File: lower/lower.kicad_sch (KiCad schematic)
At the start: 4 parts

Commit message: Lower v0.1.0. Pre-routing
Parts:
- added B1: board-outline, lower-all:board-outline-test, symbol lower-all:board-outline
- added D1: 2.7V, Diode_THT:D_T-1_P5.08mm_Horizontal, symbol Device:D_Zener
- added D2: 1N4007, Diode_THT:D_DO-41_SOD81_P10.16mm_Horizontal, symbol Diode:1N4007
- added ESCWires1, ESCWires2, ESCWires3, ESCWires4: ~, lower-all:WireESC, symbol lower-all:WireESC
- added M1, M2, M3, M4: MotorCutout, lower-all:MotorEdges, symbol lower-all:Motor
- added MotorWires1, MotorWires2, MotorWires3, MotorWires4: ~, lower-all:WireMotor, symbol lower-all:WireMotor
- added R1: 510, Resistor_SMD:R_0201_0603Metric_Pad0.64x0.40mm_HandSolder, symbol Device:R
- added R2: 33, Resistor_THT:R_Axial_DIN0207_L6.3mm_D2.5mm_P7.62mm_Horizontal, symbol Device:R
- added R3: 470, Resistor_THT:R_Axial_DIN0207_L6.3mm_D2.5mm_P7.62mm_Horizontal, symbol Device:R
- added SW1: SW_SPDT, Button_Switch_THT:SW_Slide_SPDT_Angled_CK_OS102011MA1Q, symbol Switch:SW_SPDT
- added TP1: Psense, TestPoint:TestPoint_2Pads_Pitch2.54mm_Drill0.8mm, symbol Connector:TestPoint_2Pole
- added U1: BTS50080-1TMA, Package_TO_SOT_SMD:TO-263-7_TabPin4, symbol Power_Management:BTS50080-1TMA
- added WireBatt1: ~, lower-all:WireBatt, symbol lower-all:WireBatt
- added WireESCPwr1, WireESCPwr2, WireESCPwr3, WireESCPwr4: ~, lower-all:WireESCPwr, symbol lower-all:WireESCPwr
- H1, H2, H3, H4: value MountingHole_Pad -> MountingHole; symbol Mechanical:MountingHole_Pad -> Mechanical:MountingHole
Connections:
- new net: SW1.2 (B), U1.3 (IN)
- new net: D2.2 (A), U1.5 (IS)
- new net: R2.2, R3.1
- new net A1: ESCWires1.1 (Red), MotorWires1.1 (Upper)
- new net A2: ESCWires2.1 (Red), MotorWires2.3 (Lower)
- new net A3: ESCWires3.1 (Red), MotorWires3.3 (Lower)
- new net A4: ESCWires4.1 (Red), MotorWires4.1 (Upper)
- new net B1: ESCWires1.2 (Blue), MotorWires1.2 (Middle)
- new net B2: ESCWires2.2 (Blue), MotorWires2.2 (Middle)
- new net B3: ESCWires3.2 (Blue), MotorWires3.2 (Middle)
- new net B4: ESCWires4.2 (Blue), MotorWires4.2 (Middle)
- new net C1: ESCWires1.3 (Black), MotorWires1.3 (Lower)
- new net C2: ESCWires2.3 (Black), MotorWires2.1 (Upper)
- new net C3: ESCWires3.3 (Black), MotorWires3.1 (Upper)
- new net C4: ESCWires4.3 (Black), MotorWires4.3 (Lower)
- new net GND: D1.2 (A), R1.2, R3.2, SW1.1 (A), TP1.2, WireBatt1.2 (Black), WireESCPwr1.2 (Black), WireESCPwr2.2 (Black), WireESCPwr3.2 (Black), WireESCPwr4.2 (Black)
- new net Psense: D1.1 (K), D2.1 (K), R1.1, R2.1, TP1.1
- new net Vbb: U1.4 (Vbb), WireBatt1.1 (Red)
- new net Vcc: U1.1 (OUT), U1.2 (OUT), U1.6 (OUT), U1.7 (OUT), WireESCPwr1.1 (Red), WireESCPwr2.1 (Red), WireESCPwr3.1 (Red), WireESCPwr4.1 (Red)
- no-connect marks 0 -> 1
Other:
- note added: "TODO: * Route * Redo frame shape"

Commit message: Lower v0.1.1. Pre-routing
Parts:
- added JP1: Jumper_2_Bridged, lower-all:SolderJumperLarge, symbol Jumper:Jumper_2_Bridged
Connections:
- net GND: now also JP1.2 (B); no longer WireBatt1.2 (Black), WireESCPwr1.2 (Black), WireESCPwr2.2 (Black), WireESCPwr3.2 (Black), WireESCPwr4.2 (Black)
- new net GNDPWR: JP1.1 (A), WireBatt1.2 (Black), WireESCPwr1.2 (Black), WireESCPwr2.2 (Black), WireESCPwr3.2 (Black), WireESCPwr4.2 (Black)
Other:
- note added: "TODO: * Fix rotor placement * Route * Redo frame shape"
- note removed: "TODO: * Route * Redo frame shape"
- moved on the sheet: B1, D1, D2, ESCWires1, ESCWires2, ESCWires3, ESCWires4, M1, M2, M3, M4, MotorWires1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

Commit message: Lower v0.1.2. Pre-routing
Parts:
- renumbered WireBatt1 to Batt1
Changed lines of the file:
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@@
 		(dnp no)
 		(fields_autoplaced yes)
-		(property "Reference" "WireBatt1"
+		(property "Reference" "Batt1"
 			(at 245.11 24.13 0)
 			(do_not_autoplace yes)
@@
 			(project ""
 				(path "/38495dd5-5138-4faa-88d9-26986d1150e3"
-					(reference "WireBatt1")
+					(reference "Batt1")
 					(unit 1)
 				)

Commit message: Upper/Lower: v0.2.0. Pre-routed
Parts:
- added R4, R5: 0, Resistor_SMD:R_1206_3216Metric_Pad1.30x1.75mm_HandSolder, symbol Device:R
- added R6, R7: 0, Resistor_THT:R_Axial_DIN0207_L6.3mm_D2.5mm_P7.62mm_Horizontal, symbol Device:R
- added TP2: Vsense, TestPoint:TestPoint_2Pads_Pitch2.54mm_Drill0.8mm, symbol Connector:TestPoint_2Pole
- TP1: value Psense -> Isense
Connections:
- net GND: now also R5.1, R7.2, TP2.2
- net Vcc: now also R4.1, R6.1
- net Psense renamed Isense
- new net _Vsense: R4.2, R5.2, R6.2, R7.1, TP2.1

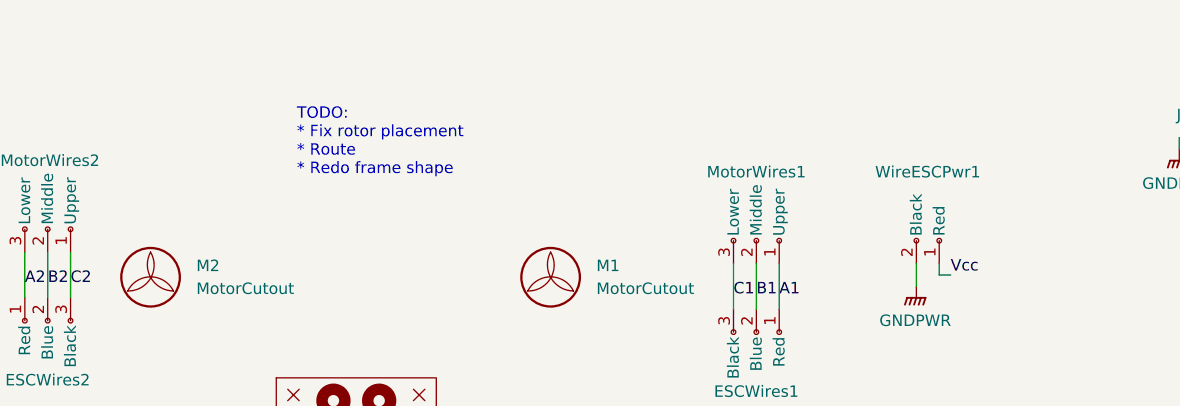
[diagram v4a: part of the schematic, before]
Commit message: Upper/Lower: Add post-assembly fixup comments
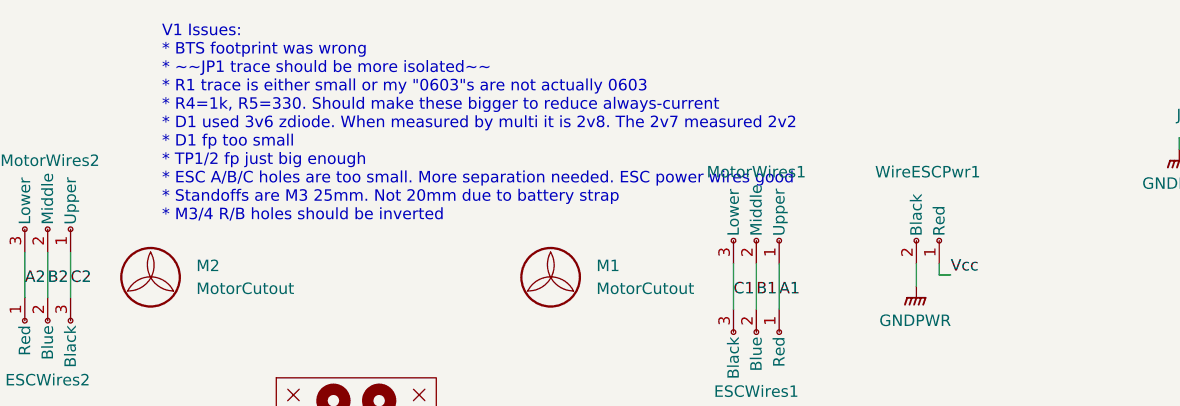
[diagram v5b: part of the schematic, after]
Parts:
- U1: footprint Package_TO_SOT_SMD:TO-263-7_TabPin4 -> Package_TO_SOT_SMD:Infineon_PG-TO-220-7Lead_TabPin8
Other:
- note added: "V1 Issues: * BTS footprint was wrong * ~~JP1 trace should be more isolated~~ * R1 trace is either small or my "0603"s are not actually 0603 * R4=1k, R5=330. Should make these bigger to reduce always-current * D1 used 3v6 zdiode. When measured by multi it is 2v8. The 2v7 measured 2v2 * D1 fp too small * TP1/2 fp just big enough * ESC A/B/C holes are too small. More separation needed. ESC power wir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"
- note removed: "TODO: * Fix rotor placement * Route * Redo frame shape"
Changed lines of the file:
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@@
 		)
 	)
-	(text "TODO:\n* Fix rotor placement\n* Route\n* Redo frame shape"
-		(exclude_from_sim no)
-		(at 98.806 25.908 0)
+	(text "V1 Issues:\n* BTS footprint was wrong\n* ~~JP1 trace should be more isolated~~\n* R1 trace is either small or my \"0603\"s are not actually 0603\n* R4=1k, R5=330. Should make these bigger to reduce always-current\n* D1 used 3v6 zdiode. When measured by multi it is 2v8. The 2v7 measured 2v2\n* D1 fp too small\n* TP1/2 fp just big enough\n* ESC A/B/C holes are too small. More separation needed. ESC power wires good\n* Standoffs are M3 25mm. Not 20mm due to battery strap\n* M3/4 R/B holes should be inverted"
+		(exclude_from_sim no)
+		(at 83.82 23.876 0)
 		(effects
 			(font
@@
 			)
 		)
-		(property "Footprint" "Package_TO_SOT_SMD:TO-263-7_TabPin4"
+		(property "Footprint" "Package_TO_SOT_SMD:Infineon_PG-TO-220-7Lead_TabPin8"
 			(at 266.7 54.61 0)
 			(effects

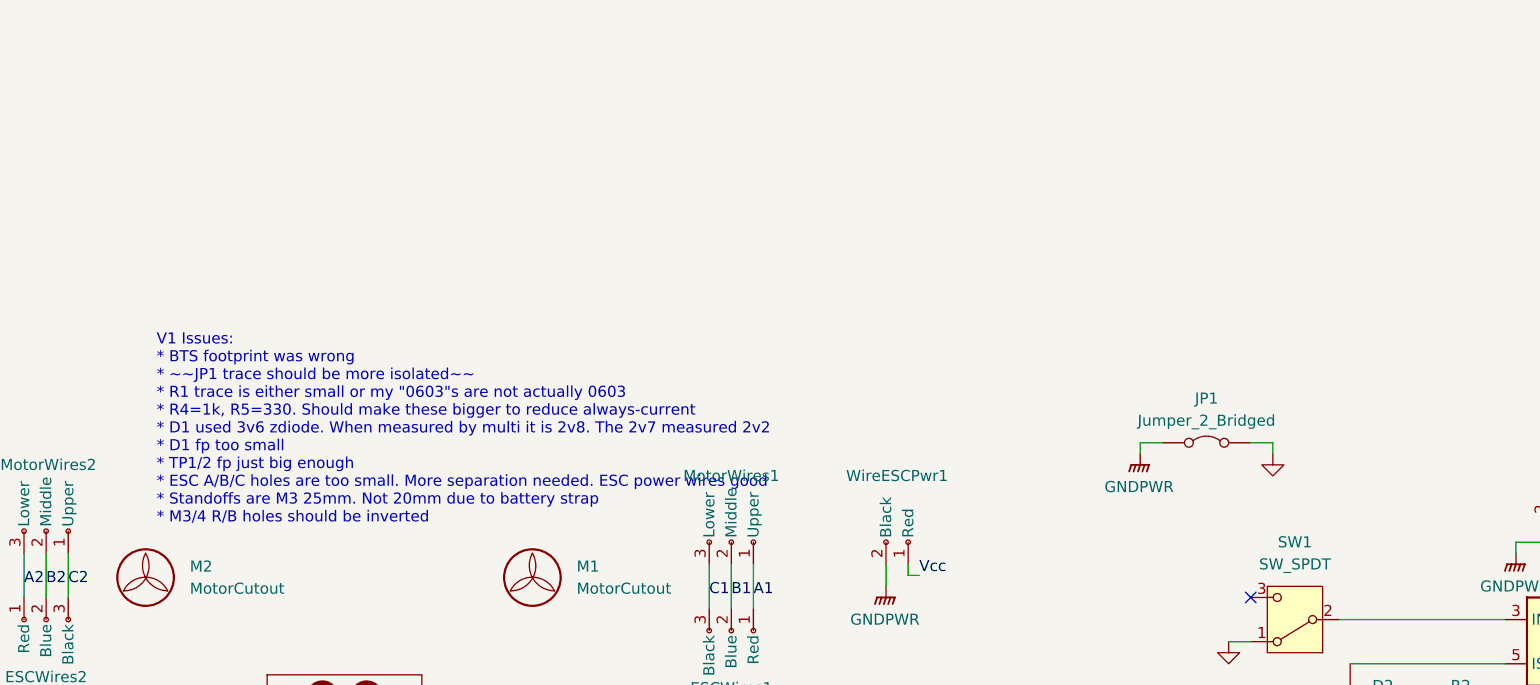
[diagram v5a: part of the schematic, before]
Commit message: Upper/Lower: Add notes
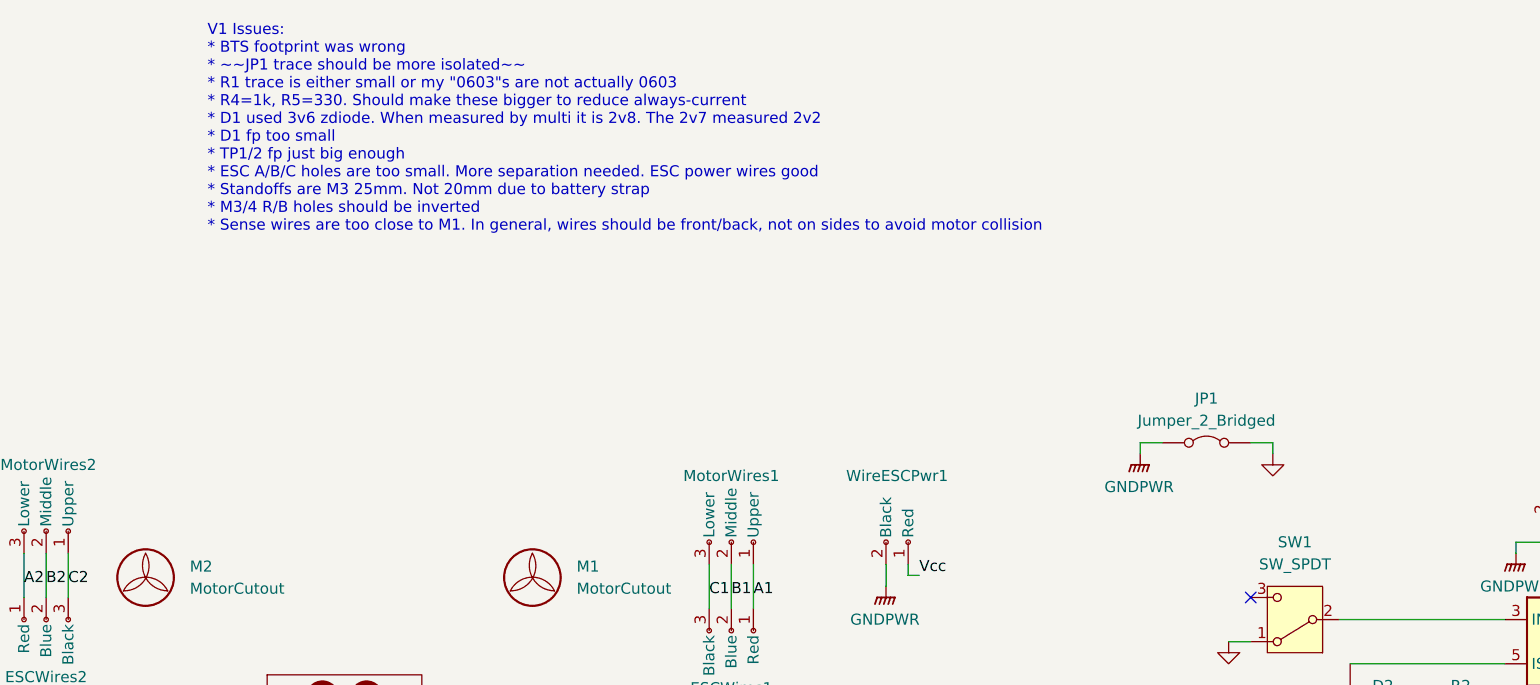
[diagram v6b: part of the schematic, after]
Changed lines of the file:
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@@
 		)
 	)
-	(text "V1 Issues:\n* BTS footprint was wrong\n* ~~JP1 trace should be more isolated~~\n* R1 trace is either small or my \"0603\"s are not actually 0603\n* R4=1k, R5=330. Should make these bigger to reduce always-current\n* D1 used 3v6 zdiode. When measured by multi it is 2v8. The 2v7 measured 2v2\n* D1 fp too small\n* TP1/2 fp just big enough\n* ESC A/B/C holes are too small. More separation needed. ESC power wires good\n* Standoffs are M3 25mm. Not 20mm due to battery strap\n* M3/4 R/B holes should be inverted"
+	(text "V1 Issues:\n* BTS footprint was wrong\n* ~~JP1 trace should be more isolated~~\n* R1 trace is either small or my \"0603\"s are not actually 0603\n* R4=1k, R5=330. Should make these bigger to reduce always-current\n* D1 used 3v6 zdiode. When measured by multi it is 2v8. The 2v7 measured 2v2\n* D1 fp too small\n* TP1/2 fp just big enough\n* ESC A/B/C holes are too small. More separation needed. ESC power wires good\n* Standoffs are M3 25mm. Not 20mm due to battery strap\n* M3/4 R/B holes should be inverted\n* Sense wires are too close to M1. In general, wires should be front/back, not on sides to avoid motor collision"
 		(exclude_from_sim no)
-		(at 83.82 23.876 0)
+		(at 89.662 -10.668 0)
 		(effects
 			(font
